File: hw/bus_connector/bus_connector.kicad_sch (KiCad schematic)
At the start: 10 parts, among them J1 DE9_Left, J2 DE9_Top, J3 DE9_Right

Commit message: Add  docs
Signed-off-by: Mateusz Pająk <22417805+Tai-Min@users.noreply.github.com>
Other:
- note added: "This documentation describes Open Hardware and is licensed under the CERN OHL v. 1.2. You may redistribute and modify this documentation under the terms of the CERN OHL v.1.2.(http://ohwr.org/cernohl). This documentation is distributed WITHOUT ANY EXPRESS OR IMPLIED WARRANTY, INCLUDING OF MERCHANTABILITY, SATISFACTORY QUALITY AND FITNESS FOR A PARTICULAR PURPOSE. Please see the CERN OHL v.1.2 for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"
- title: (none) -> Bus Connector
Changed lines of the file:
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@@
 	(generator_version "9.0")
 	(paper "A4")
+	(title_block
+		(title "Bus Connector")
+		(date "2025-11-24")
+		(rev "1.0")
+	)
 	(rectangle
 		(start 152.4 91.44)
@@
 		(effects
 			(font
+				(size 1.27 1.27)
+			)
+		)
+	)
+	(text "This documentation describes Open Hardware and is licensed under the CERN OHL v. 1.2.\nYou may redistribute and modify this documentation under the terms of the \nCERN OHL v.1.2.(http://ohwr.org/cernohl). This documentation is distributed \nWITHOUT ANY EXPRESS OR IMPLIED WARRANTY, INCLUDING OF MERCHANTABILITY,\nSATISFACTORY QUALITY AND FITNESS FOR A PARTICULAR PURPOSE.\nPlease see the CERN OHL v.1.2 for applicable conditions"
+		(exclude_from_sim no)
+		(at 231.394 174.244 0)
+		(effects
+			(font

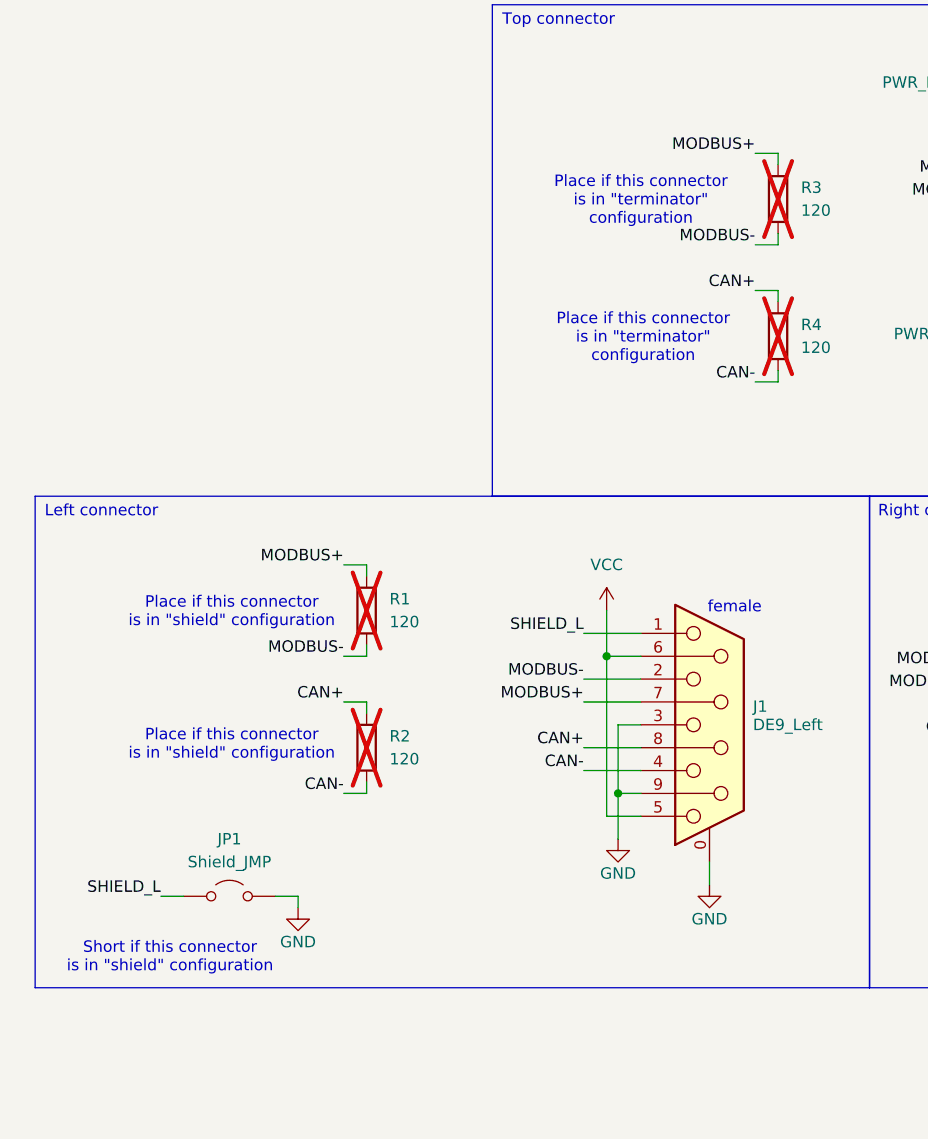
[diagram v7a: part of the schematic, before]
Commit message: Add QR code, remove shield jumper
Signed-off-by: Mateusz Pająk <22417805+Tai-Min@users.noreply.github.com>
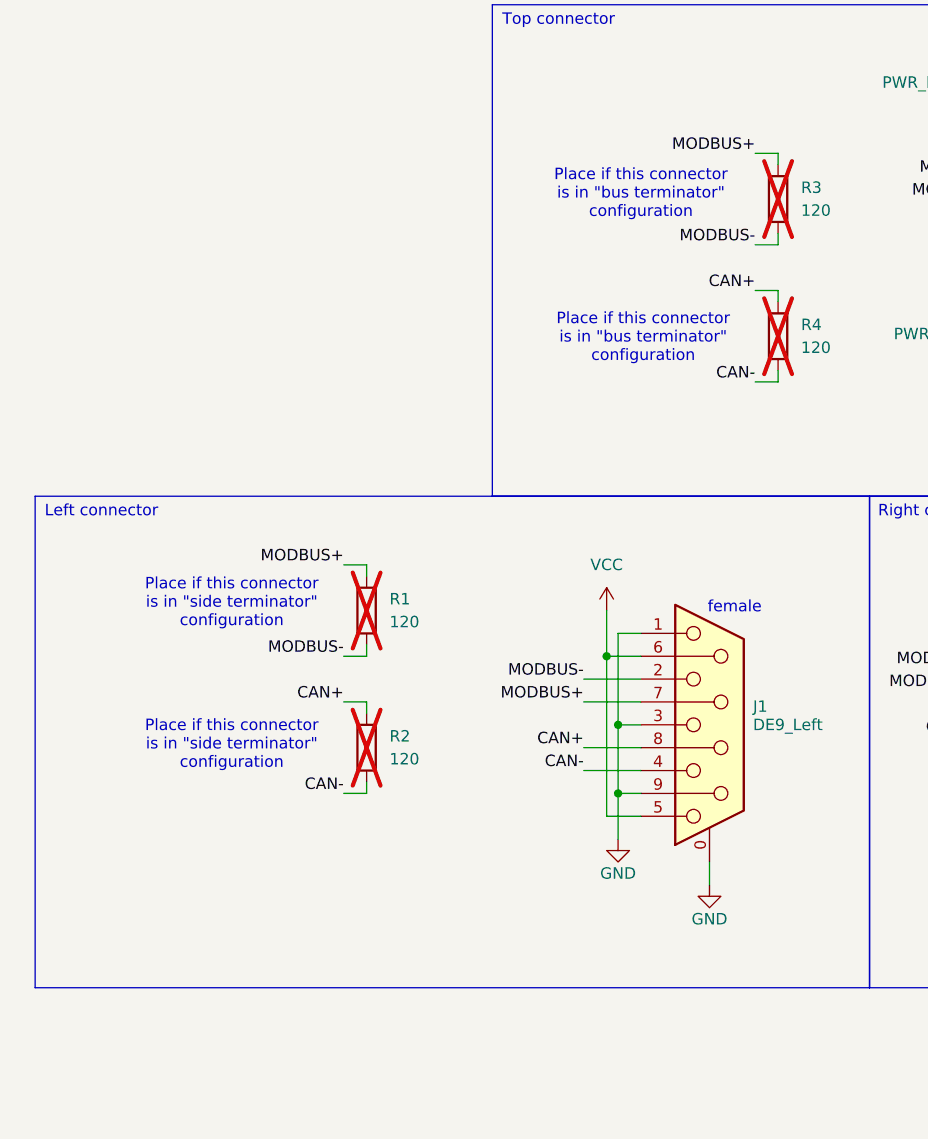
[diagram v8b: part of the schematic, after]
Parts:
- removed JP1: Shield_JMP, Jumper:SolderJumper-2_P1.3mm_Open_RoundedPad1.0x1.5mm, symbol Jumper:Jumper_2_Open
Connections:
- net SHIELD_L is gone; now on net GND: J1.1
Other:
- note added: "Place if this connector is in "bus terminator" configuration"
- note added: "Place if this connector is in "side terminator" configuration"
- note removed: "Place if this connector is in "shield" configuration"
- note removed: "Short if this connector is in "shield" configuration"
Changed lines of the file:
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@@
 		)
 	)
-	(text "Place if this connector\nis in \"shield\" configuration"
-		(exclude_from_sim no)
-		(at 81.534 104.394 0)
+	(text "Place if this connector\nis in \"side terminator\"\nconfiguration"
+		(exclude_from_sim no)
+		(at 81.534 103.378 0)
 		(effects
 			(font
@@
 		)
 	)
-	(text "Place if this connector\nis in \"shield\" configuration"
+	(text "Place if this connector\nis in \"side terminator\"\nconfiguration"
 		(exclude_from_sim no)
 		(at 81.534 119.126 0)
@@
 		)
 	)
+	(text "Place if this connector\nis in \"bus terminator\" \nconfiguration"
+		(exclude_from_sim no)
+		(at 127 57.912 0)
+		(effects
+			(font
+				(size 1.27 1.27)
+			)
+		)
+	)
 	(text "Place if this connector\nis in \"terminator\" \nconfiguration"
 		(exclude_from_sim no)
-		(at 127 58.674 0)
-		(effects
-			(font
-				(size 1.27 1.27)
-			)
-		)
-	)
-	(text "Place if this connector\nis in \"terminator\" \nconfiguration"
-		(exclude_from_sim no)
 		(at 185.674 140.716 0)
 		(effects
@@
 		)
 	)
-	(text "Short if this connector\nis in \"shield\" configuration"
-		(exclude_from_sim no)
-		(at 74.676 142.748 0)
-		(effects
-			(font
-				(size 1.27 1.27)
-			)
-		)
-	)
 	(text "female"
 		(exclude_from_sim no)
@@
 		)
 	)
-	(text "Place if this connector\nis in \"terminator\" \nconfiguration"
+	(text "Place if this connector\nis in \"bus terminator\" \nconfiguration"
 		(exclude_from_sim no)
 		(at 127.254 73.914 0)
@@
 	)
 	(junction
+		(at 124.46 116.84)
+		(diameter 0)
+		(color 0 0 0 0)
+	)
+	(junction
 		(at 187.96 110.49)
 		(diameter 0)
@@
 	(wire
 		(pts
+			(xy 124.46 106.68) (xy 124.46 116.84)
+		)
+		(stroke
+			(width 0)
+			(type default)
+		)
+	)
+	(wire
+		(pts
 			(xy 208.28 113.03) (xy 217.17 113.03)
 		)
@@
 	(wire
 		(pts
-			(xy 88.9 135.89) (xy 88.9 137.16)
-		)
-		(stroke
-			(width 0)
-			(type default)
-		)
-	)
-	(wire
-		(pts
-			(xy 86.36 135.89) (xy 88.9 135.89)
-		)
-		(stroke
-			(width 0)
-			(type default)
-		)
-	)
-	(wire
-		(pts
 			(xy 170.18 60.96) (xy 170.18 68.58)
 		)
@@
 	(wire
 		(pts
-			(xy 120.65 106.68) (xy 127 106.68)
-		)
-		(stroke
-			(width 0)
-			(type default)
-		)
-	)
-	(wire
-		(pts
 			(xy 166.37 55.88) (xy 172.72 55.88)
 		)
@@
 	(wire
 		(pts
+			(xy 124.46 106.68) (xy 127 106.68)
+		)
+		(stroke
+			(width 0)
+			(type default)
+		)
+	)
+	(wire
+		(pts
 			(xy 208.28 130.81) (xy 207.01 130.81)
 		)
@@
 	(wire
 		(pts
-			(xy 73.66 135.89) (xy 76.2 135.89)
-		)
-		(stroke
-			(width 0)
-			(type default)
-		)
-	)
-	(wire
-		(pts
 			(xy 186.69 120.65) (xy 217.17 120.65)
 		)
@@
 			(width 0)
 			(type default)
-		)
-	)
-	(label "SHIELD_L"
-		(at 120.65 106.68 180)
-		(effects
-			(font
-				(size 1.27 1.27)
-			)
-			(justify right bottom)
 		)
 	)
@@
 	(label "MODBUS-"
 		(at 166.37 55.88 180)
-		(effects
-			(font
-				(size 1.27 1.27)
-			)
-			(justify right bottom)
-		)
-	)
-	(label "SHIELD_L"
-		(at 73.66 135.89 180)
 		(effects
 			(font
@@
 	)
 	(symbol
-		(lib_id "Jumper:Jumper_2_Open")
-		(at 81.28 135.89 0)
-		(unit 1)
-		(exclude_from_sim no)
-		(in_bom yes)
-		(on_board yes)
-		(dnp no)
-		(fields_autoplaced yes)
-		(property "Reference" "JP1"
-			(at 81.28 129.54 0)
-			(effects
-				(font
-					(size 1.27 1.27)
-				)
-			)
-		)
-		(property "Value" "Shield_JMP"
-			(at 81.28 132.08 0)
-			(effects
-				(font
-					(size 1.27 1.27)
-				)
-			)
-		)
-		(property "Footprint" "Jumper:SolderJumper-2_P1.3mm_Open_RoundedPad1.0x1.5mm"
-			(at 81.28 135.89 0)
-			(effects
-				(font
-					(size 1.27 1.27)
-				)
-				(hide yes)
-			)
-		)
-		(property "Datasheet" "~"
-			(at 81.28 135.89 0)
-			(effects
-				(font
-					(size 1.27 1.27)
-				)
-				(hide yes)
-			)
-		)
-		(property "Description" "Jumper, 2-pole, open"
-			(at 81.28 135.89 0)
-			(effects
-				(font
-					(size 1.27 1.27)
-				)
-				(hide yes)
-			)
-		)
-		(pin "1"
-		)
-		(pin "2"
-		)
-		(instances
-			(project "terminator"
-				(path "/e42bcc36-c7d3-414a-8e1a-42e6cdd67034"
-					(reference "JP1")
-					(unit 1)
-				)
-			)
-		)
-	)
-	(symbol
 		(lib_id "Diode:SM712_SOT23")
 		(at 198.12 130.81 0)
@@
 					(unit 1)
 				)
-			)
-		)
-	)
-	(symbol
-		(lib_id "power:GND")
-		(at 88.9 137.16 0)
-		(unit 1)
-		(exclude_from_sim no)
-		(in_bom yes)
-		(on_board yes)
-		(dnp no)
-		(property "Reference" "#PWR01"
-			(at 88.9 143.51 0)
-			(effects
-				(font
-					(size 1.27 1.27)
-				)
-				(hide yes)
-			)
-		)
-		(property "Value" "GND"
-			(at 88.9 140.97 0)
-			(effects
-				(font
-					(size 1.27 1.27)
-				)
-			)
-		)
-		(property "Footprint" ""
-			(at 88.9 137.16 0)
-			(effects
-				(font
-					(size 1.27 1.27)
-				)
-				(hide yes)
-			)
-		)
-		(property "Datasheet" ""
-			(at 88.9 137.16 0)
-			(effects
-				(font
-					(size 1.27 1.27)
-				)
-				(hide yes)
-			)
-		)
-		(property "Description" "Power symbol creates a global label with name \"GND\" , ground"
-			(at 88.9 137.16 0)
-			(effects
-				(font
-					(size 1.27 1.27)
-				)
-				(hide yes)
-			)
-		)
-		(pin "1"
-		)
-		(instances
-			(project "terminator"
-				(path "/e42bcc36-c7d3-414a-8e1a-42e6cdd67034"
-					(reference "#PWR01")
-					(unit 1)
-				)
